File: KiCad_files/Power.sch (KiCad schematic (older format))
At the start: 76 parts, among them J2 PCIe_6_Pin_Power, Q1 Q_NMOS_DGS, Q2 Q_PMOS_DGS, U1 XC7A35T_CSG325, U2 MAX15027, U3 PI3420, U4 PI3421, U5 PI3420

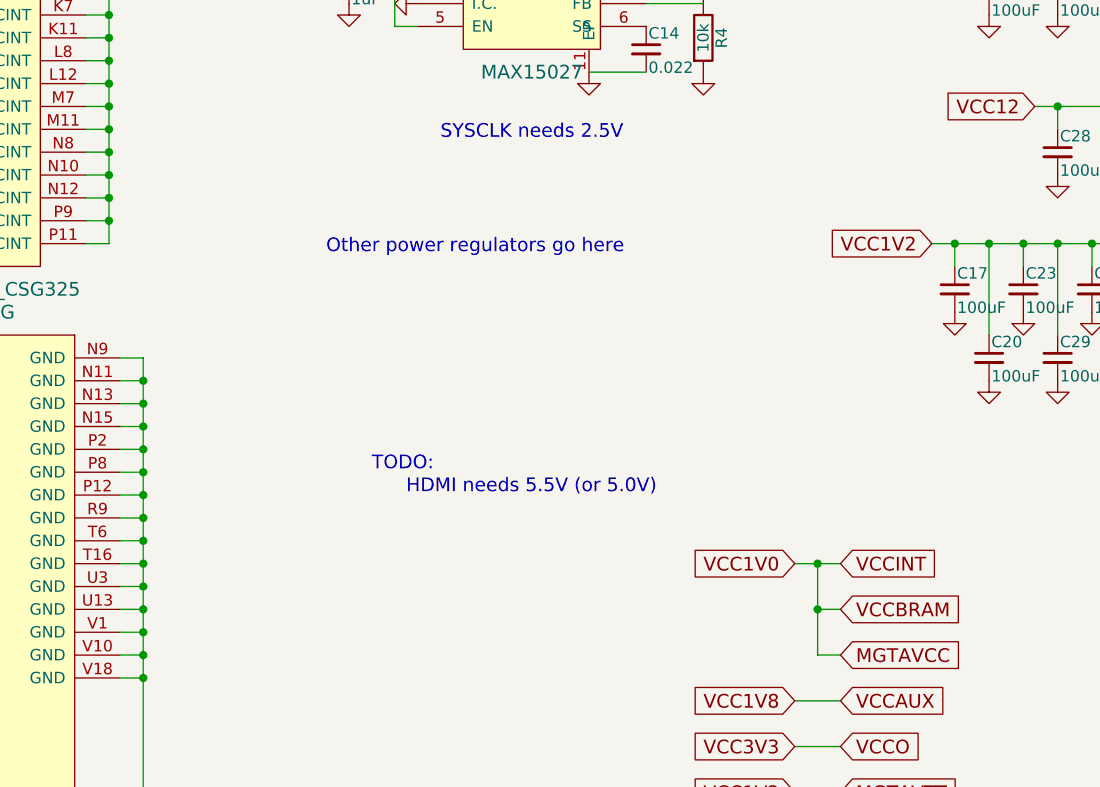
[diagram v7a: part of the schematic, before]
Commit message: Added 5V supply for HDMI.
Added jumper for USB-C power
TODO:
Add more jumpers (EMCCLK and Config)
Add lots of test points
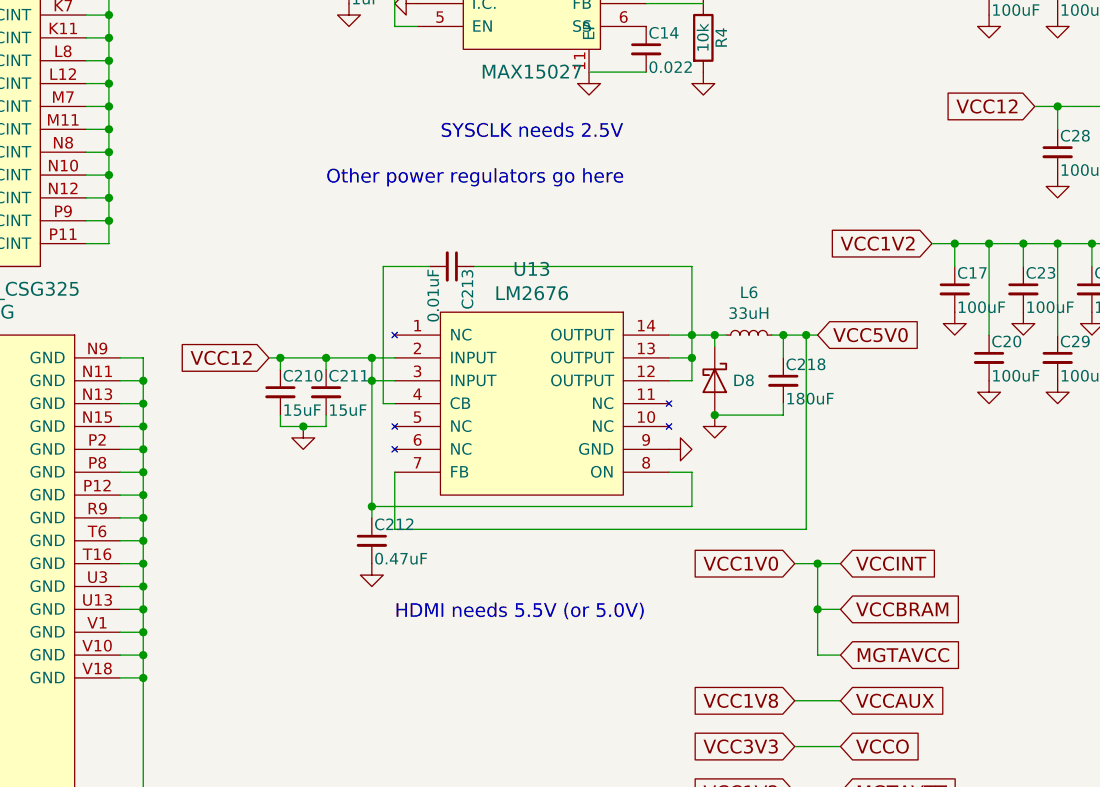
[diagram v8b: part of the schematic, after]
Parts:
- added C210, C211: 15uF, symbol Device:C_Small
- added C212: 0.47uF, symbol Device:C_Small
- added C213: 0.01uF, symbol Device:C_Small
- added C218: 180uF, symbol Device:C_Small
- added D8: D_Schottky, symbol Device:D_Schottky
- added L6: 33uH, symbol Device:L_Small
- added U13: LM2676, symbol custom:LM2676
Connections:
- net GND: now also C210.2, C211.2, C212.2, C218.2, D8.2 (A), U13.9 (GND)
- net PCIe_12V: now also C210.1, C211.1, C212.1, U13.2 (INPUT), U13.3 (INPUT), U13.8 (ON)
- new net: C213.1, D8.1 (K), L6.1, U13.12 (OUTPUT), U13.13 (OUTPUT), U13.14 (OUTPUT)
- new net: C213.2, U13.4 (CB)
- new net VCC5V0: C218.1, L6.2, U13.7 (FB)
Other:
- note removed: "TODO:"
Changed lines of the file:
@@
 Text Notes 8150 6450 0    60   ~ 0
 Use  NMOS with 1.7V V_threshhold and PMOS with > 3A output
-Text Notes 4000 4850 0    60   ~ 0
+Text Notes 4000 4550 0    60   ~ 0
 Other power regulators go here
 Text Notes 8850 3850 0    60   ~ 0
@@
 Wire Wire Line
 	4300 3650 4300 3850
-Text Notes 4350 5900 0    60   ~ 0
+Text Notes 4300 6450 0    60   ~ 0
 HDMI needs 5.5V (or 5.0V)
-Text Notes 4200 5800 0    60   ~ 0
-TODO:
 NoConn ~ 9900 2400
 NoConn ~ 9900 4000
@@
 Wire Wire Line
 	9700 5950 9900 5950
+$Comp
+L custom:LM2676 U13
+U 1 1 5C81CD56
+P 4900 5700
+F 0 "U13" H 4900 6487 60  0000 C CNN
+F 1 "LM2676" H 4900 6381 60  0000 C CNN
+F 2 "" H 4900 5850 60  0001 C CNN
+F 3 "" H 4900 5850 60  0001 C CNN
+	1    4900 5700
+	1    0    0    -1
+$EndComp
+$Comp
+L power:GND #PWR0133
+U 1 1 5C81D209
+P 5500 5700
+F 0 "#PWR0133" H 5500 5450 50  0001 C CNN
+F 1 "GND" H 5500 5550 50  0001 C CNN
+F 2 "" H 5500 5700 50  0001 C CNN
+F 3 "" H 5500 5700 50  0001 C CNN
+	1    5500 5700
+	0    -1   -1   0
+$EndComp
+Wire Wire Line
+	4200 5950 4200 5400
+Wire Wire Line
+	4200 5300 4300 5300
+Wire Wire Line
+	4300 5400 4200 5400
+Connection ~ 4200 5400
+Wire Wire Line
+	4200 5400 4200 5300
+Wire Wire Line
+	5500 5800 5600 5800
+Wire Wire Line
+	5600 5800 5600 5950
+Wire Wire Line
+	4200 5950 5600 5950
+Text GLabel 3750 5300 0    60   Input ~ 0
+VCC12
+Connection ~ 4200 5300
+Text GLabel 6150 5200 2    60   Input ~ 0
+VCC5V0
+Wire Wire Line
+	5500 5200 5600 5200
+Wire Wire Line
+	5600 5200 5600 5300
+Wire Wire Line
+	5600 5400 5500 5400
+Connection ~ 5600 5200
+Wire Wire Line
+	5600 5200 5700 5200
+Wire Wire Line
+	5500 5300 5600 5300
+Connection ~ 5600 5300
+Wire Wire Line
+	5600 5300 5600 5400
+$Comp
+L Device:C_Small C210
+U 1 1 5C7B6C9B
+P 3800 5450
+F 0 "C210" H 3810 5520 50  0000 L CNN
+F 1 "15uF" H 3810 5370 50  0000 L CNN
+F 2 "" H 3800 5450 50  0001 C CNN
+F 3 "" H 3800 5450 50  0001 C CNN
+	1    3800 5450
+	1    0    0    -1
+$EndComp
+$Comp
+L Device:C_Small C211
+U 1 1 5C7B733D
+P 4000 5450
+F 0 "C211" H 4010 5520 50  0000 L CNN
+F 1 "15uF" H 4010 5370 50  0000 L CNN
+F 2 "" H 4000 5450 50  0001 C CNN
+F 3 "" H 4000 5450 50  0001 C CNN
+	1    4000 5450
+	1    0    0    -1
+$EndComp
+$Comp
+L Device:C_Small C212
+U 1 1 5C7B740B
+P 4200 6100
+F 0 "C212" H 4210 6170 50  0000 L CNN
+F 1 "0.47uF" H 4210 6020 50  0000 L CNN
+F 2 "" H 4200 6100 50  0001 C CNN
+F 3 "" H 4200 6100 50  0001 C CNN
+	1    4200 6100
+	1    0    0    -1
+$EndComp
+$Comp
+L power:GND #PWR0132
+U 1 1 5C7B75E7
+P 4200 6200
+F 0 "#PWR0132" H 4200 5950 50  0001 C CNN
+F 1 "GND" H 4200 6050 50  0001 C CNN
+F 2 "" H 4200 6200 50  0001 C CNN
+F 3 "" H 4200 6200 50  0001 C CNN
+	1    4200 6200
+	1    0    0    -1
+$EndComp
+Wire Wire Line
+	4200 6000 4200 5950
+Connection ~ 4200 5950
+$Comp
+L power:GND #PWR0131
+U 1 1 5C813FA2
+P 3900 5600
+F 0 "#PWR0131" H 3900 5350 50  0001 C CNN
+F 1 "GND" H 3900 5450 50  0001 C CNN
+F 2 "" H 3900 5600 50  0001 C CNN
+F 3 "" H 3900 5600 50  0001 C CNN
+	1    3900 5600
+	1    0    0    -1
+$EndComp
+Wire Wire Line
+	4000 5350 4000 5300
+Connection ~ 4000 5300
+Wire Wire Line
+	4000 5300 4200 5300
+Wire Wire Line
+	4000 5550 4000 5600
+Wire Wire Line
+	4000 5600 3900 5600
+Wire Wire Line
+	3750 5300 3800 5300
+Wire Wire Line
+	3800 5550 3800 5600
+Wire Wire Line
+	3800 5600 3900 5600
+Connection ~ 3900 5600
+Wire Wire Line
+	3800 5350 3800 5300
+Connection ~ 3800 5300
+Wire Wire Line
+	3800 5300 4000 5300
+$Comp
+L Device:C_Small C213
+U 1 1 5C963D14
+P 4550 4900
+F 0 "C213" H 4560 4970 50  0000 L CNN
+F 1 "0.01uF" H 4560 4820 50  0000 L CNN
+F 2 "" H 4550 4900 50  0001 C CNN
+F 3 "" H 4550 4900 50  0001 C CNN
+	1    4550 4900
+	0    1    1    0
+$EndComp
+Wire Wire Line
+	4300 5500 4250 5500
+Wire Wire Line
+	4250 5500 4250 4900
+Wire Wire Line
+	4250 4900 4450 4900
+Wire Wire Line
+	4650 4900 5600 4900
+Wire Wire Line
+	5600 4900 5600 5200
+$Comp
+L Device:D_Schottky D8
+U 1 1 5C9C687A
+P 5700 5400
+F 0 "D8" V 5700 5479 50  0000 L CNN
+F 1 "D_Schottky" V 5745 5479 50  0001 L CNN
+F 2 "" H 5700 5400 50  0001 C CNN
+F 3 "~" H 5700 5400 50  0001 C CNN
+	1    5700 5400
+	0    1    1    0
+$EndComp
+Wire Wire Line
+	5700 5200 5700 5250
+$Comp
+L power:GND #PWR0134
+U 1 1 5C9F826A
+P 5700 5550
+F 0 "#PWR0134" H 5700 5300 50  0001 C CNN
+F 1 "GND" H 5700 5400 50  0001 C CNN
+F 2 "" H 5700 5550 50  0001 C CNN
+F 3 "" H 5700 5550 50  0001 C CNN
+	1    5700 5550
+	1    0    0    -1
+$EndComp
+$Comp
+L Device:L_Small L6
+U 1 1 5C9F8401
+P 5850 5200
+F 0 "L6" V 6035 5200 50  0000 C CNN
+F 1 "33uH" V 5944 5200 50  0000 C CNN
+F 2 "" H 5850 5200 50  0001 C CNN
+F 3 "~" H 5850 5200 50  0001 C CNN
+	1    5850 5200
+	0    -1   -1   0
+$EndComp
+Wire Wire Line
+	5750 5200 5700 5200
+Connection ~ 5700 5200
+Wire Wire Line
+	5950 5200 6000 5200
+$Comp
+L Device:C_Small C218
+U 1 1 5CA5C600
+P 6000 5400
+F 0 "C218" H 6010 5470 50  0000 L CNN
+F 1 "180uF" H 6010 5320 50  0000 L CNN
+F 2 "" H 6000 5400 50  0001 C CNN
+F 3 "" H 6000 5400 50  0001 C CNN
+	1    6000 5400
+	1    0    0    -1
+$EndComp
+Wire Wire Line
+	6000 5500 6000 5550
+Wire Wire Line
+	6000 5550 5700 5550
+Connection ~ 5700 5550
+Wire Wire Line
+	6000 5300 6000 5200
+Connection ~ 6000 5200
+Wire Wire Line
+	6000 5200 6100 5200
+Wire Wire Line
+	6100 5200 6100 6050
+Wire Wire Line
+	6100 6050 4300 6050
+Wire Wire Line
+	4300 6050 4300 5800
+Connection ~ 6100 5200
+Wire Wire Line
+	6100 5200 6150 5200
 $EndSCHEMATC
